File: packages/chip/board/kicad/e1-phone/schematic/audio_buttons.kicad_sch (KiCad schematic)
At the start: 0 parts

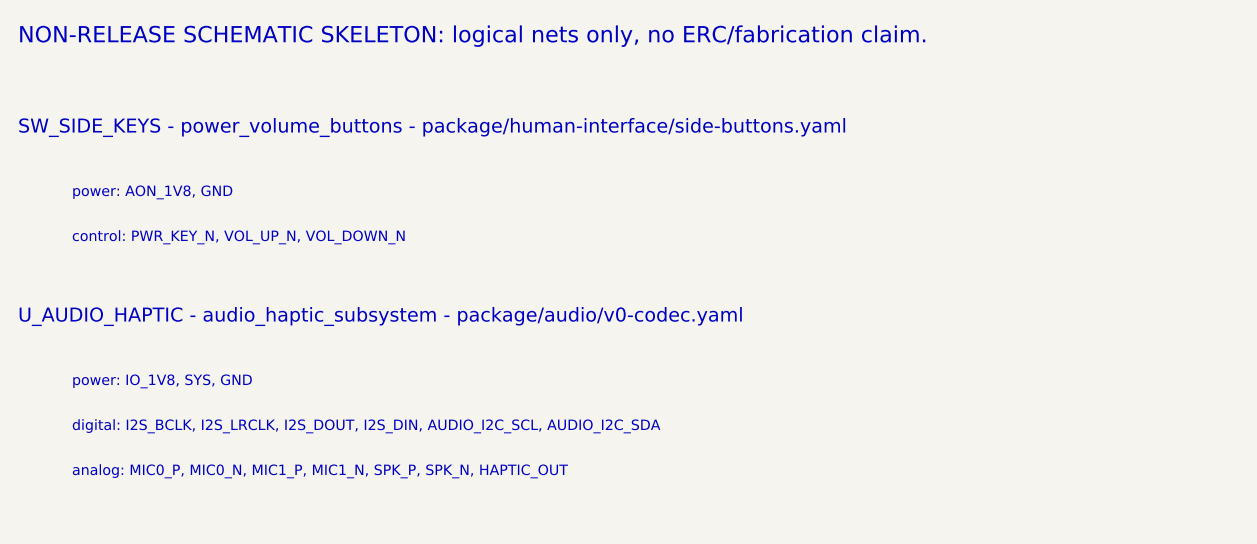
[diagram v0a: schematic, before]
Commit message: Prepare chip package for publishing
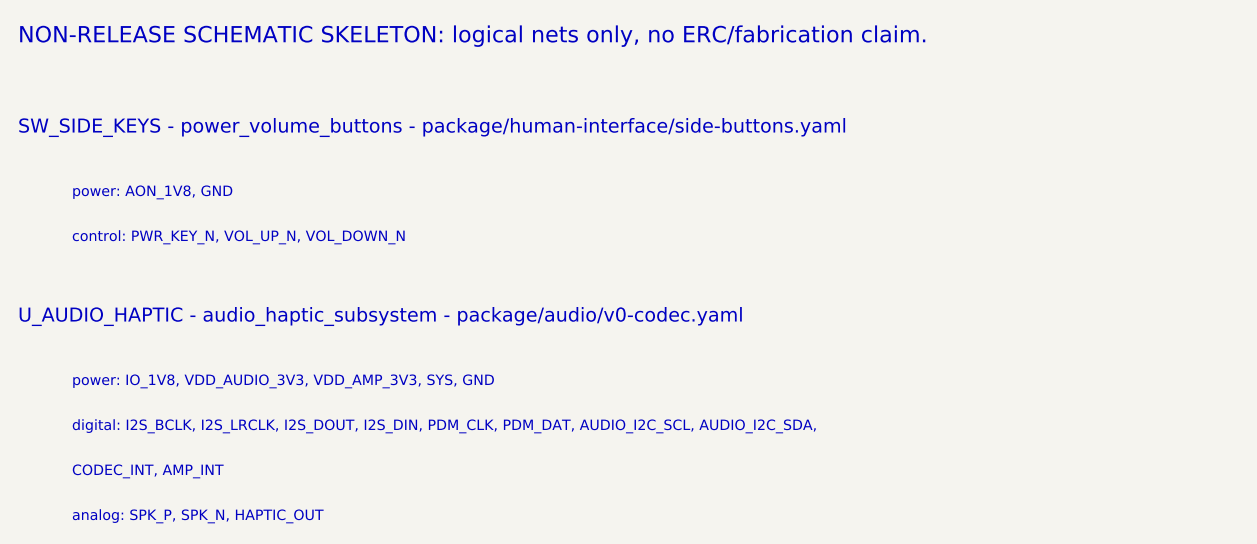
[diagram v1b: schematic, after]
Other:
- note added: "CODEC_INT, AMP_INT"
- note added: "analog: SPK_P, SPK_N, HAPTIC_OUT"
- note added: "digital: I2S_BCLK, I2S_LRCLK, I2S_DOUT, I2S_DIN, PDM_CLK, PDM_DAT, AUDIO_I2C_SCL, AUDIO_I2C_SDA,"
- note added: "power: IO_1V8, VDD_AUDIO_3V3, VDD_AMP_3V3, SYS, GND"
- note removed: "analog: MIC0_P, MIC0_N, MIC1_P, MIC1_N, SPK_P, SPK_N, HAPTIC_OUT"
- note removed: "digital: I2S_BCLK, I2S_LRCLK, I2S_DOUT, I2S_DIN, AUDIO_I2C_SCL, AUDIO_I2C_SDA"
- note removed: "power: IO_1V8, SYS, GND"
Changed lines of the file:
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@@
     (effects (font (size 1.55 1.55)) (justify left bottom))
   )
-  (text "power: IO_1V8, SYS, GND" (at 26.00 58.00 0)
+  (text "power: IO_1V8, VDD_AUDIO_3V3, VDD_AMP_3V3, SYS, GND" (at 26.00 58.00 0)
     (effects (font (size 1.15 1.15)) (justify left bottom))
   )
-  (text "digital: I2S_BCLK, I2S_LRCLK, I2S_DOUT, I2S_DIN, AUDIO_I2C_SCL, AUDIO_I2C_SDA" (at 26.00 63.00 0)
+  (text "digital: I2S_BCLK, I2S_LRCLK, I2S_DOUT, I2S_DIN, PDM_CLK, PDM_DAT, AUDIO_I2C_SCL, AUDIO_I2C_SDA," (at 26.00 63.00 0)
     (effects (font (size 1.15 1.15)) (justify left bottom))
   )
-  (text "analog: MIC0_P, MIC0_N, MIC1_P, MIC1_N, SPK_P, SPK_N, HAPTIC_OUT" (at 26.00 68.00 0)
+  (text "CODEC_INT, AMP_INT" (at 26.00 68.00 0)
     (effects (font (size 1.15 1.15)) (justify left bottom))
   )
+  (text "analog: SPK_P, SPK_N, HAPTIC_OUT" (at 26.00 73.00 0)
+    (effects (font (size 1.15 1.15)) (justify left bottom))
+  )
